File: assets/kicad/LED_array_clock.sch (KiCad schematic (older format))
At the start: 72 parts, among them U1 ULN2003A, U2 PIC16F628A, U3 74HC595, U4 74HC595

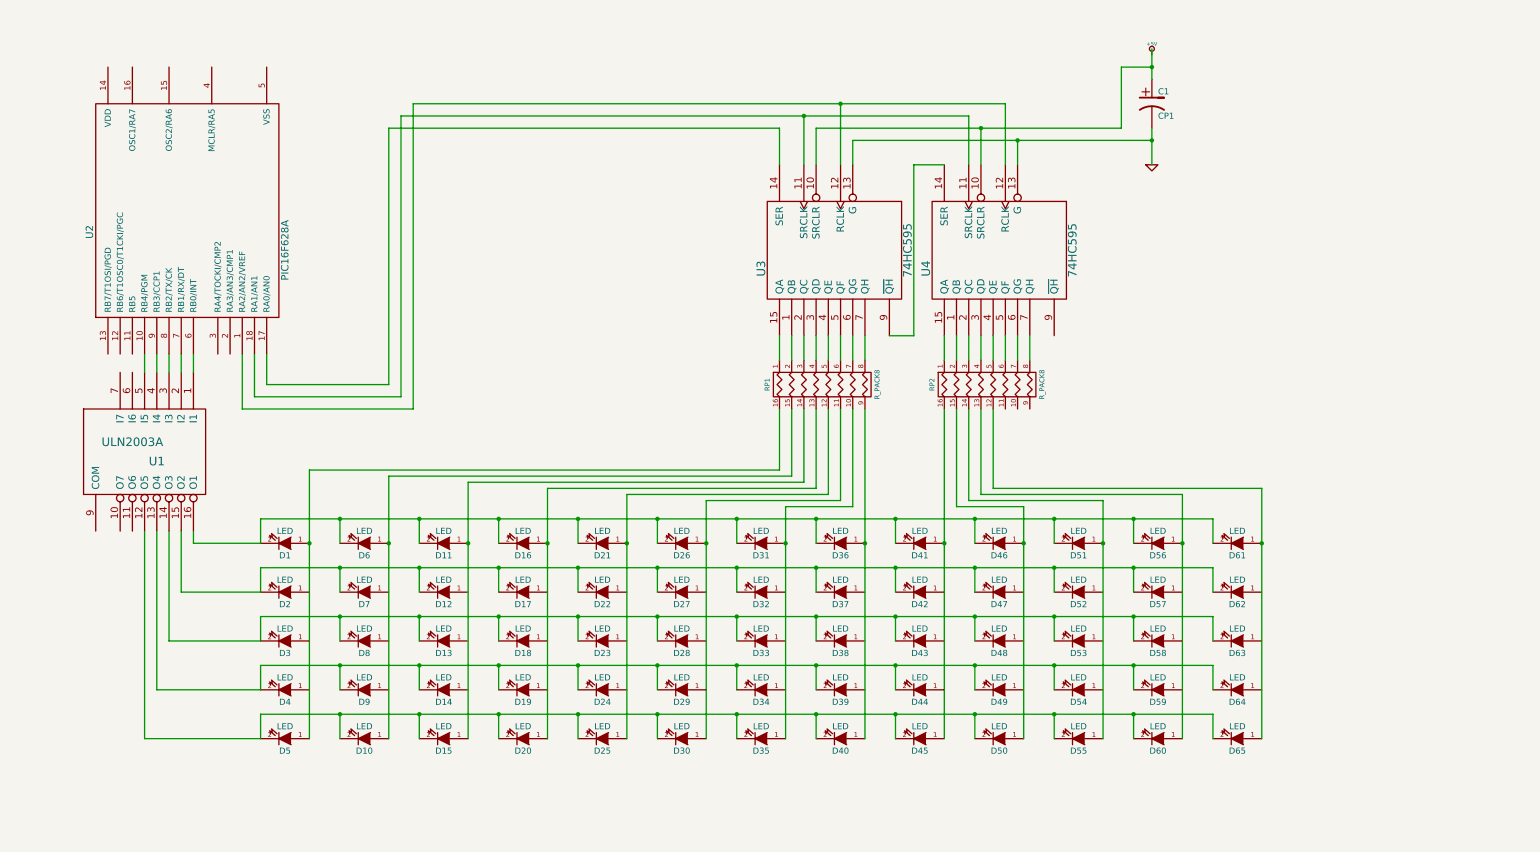
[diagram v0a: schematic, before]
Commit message: Added 3 matrix columns. Added RTC and interface components
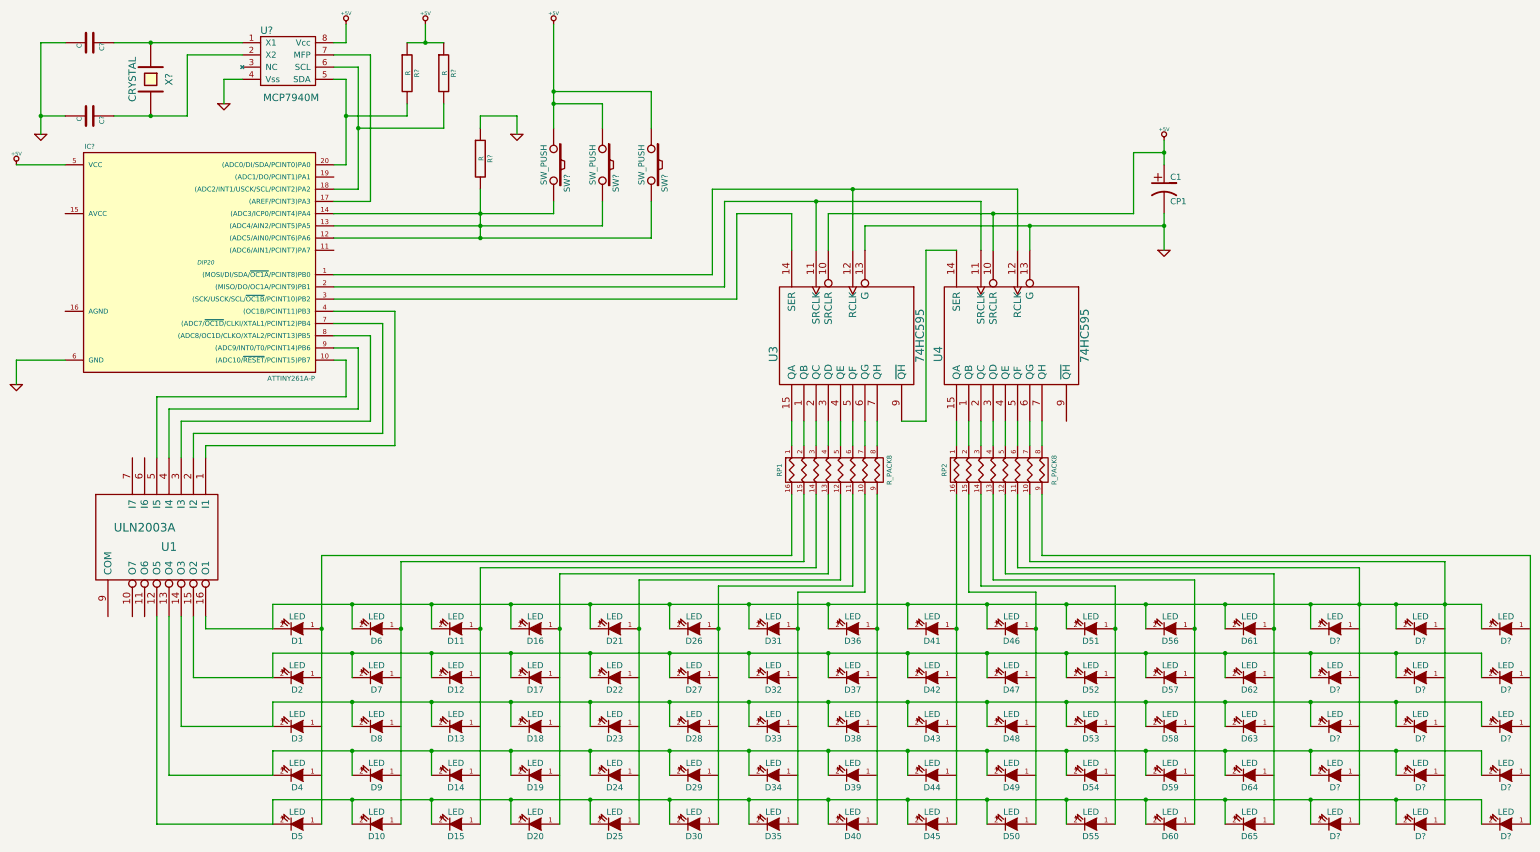
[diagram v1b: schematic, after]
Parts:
- removed U2: PIC16F628A, symbol PIC16F628A
- added C? (x2): C, ~, symbol C
- added D? (x15): LED, ~, symbol LED
- added IC?: ATTINY261A-P, DIP20, symbol ATTINY261A-P
- added R? (x3): R, ~, symbol R
- added SW? (x3): SW_PUSH, ~, symbol SW_PUSH
- added U?: MCP7940M, symbol MCP7940M
- added X?: CRYSTAL, ~, symbol CRYSTAL
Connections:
- net +5V: now also C1.1, U3.10 (SRCLR), U4.10 (SRCLR), IC?.5 (VCC), R?.1, R?.1, SW?.1, SW?.1, SW?.1, U?.8 (Vcc)
- net GND: now also C?.2, C?.2, IC?.6 (GND), R?.1, U?.4 (Vss)
- net at U3.11 (SRCLK), U4.11 (SRCLK): now also IC?.2 ((MISO/DO/OC1A/PCINT9)PB1)
- net at U3.12 (RCLK), U4.12 (RCLK): now also IC?.1 ((MOSI/DI/SDA/~OC1A~/PCINT8)PB0)
- net at U3.14 (SER): now also IC?.3 ((SCK/USCK/SCL/~OC1B~/PCINT10)PB2)
- net at D1.2 (K), D11.2 (K), D16.2 (K)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: now also RP2.10 (R7), RP2.11 (R6), D?.1 (A), D?.1 (A), D?.2 (K), D?.2 (K), D?.2 (K)
- net at D12.2 (K), D17.2 (K), D2.2 (K)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: now also D?.2 (K), D?.2 (K), D?.2 (K)
- net at D13.2 (K), D18.2 (K), D23.2 (K)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: now also D?.2 (K), D?.2 (K), D?.2 (K)
- net at D14.2 (K), D19.2 (K), D24.2 (K)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: now also D?.2 (K), D?.2 (K), D?.2 (K)
- net at D10.2 (K), D15.2 (K), D20.2 (K)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: now also D?.2 (K), D?.2 (K), D?.2 (K)
- net at RP2.9 (R8): now also D?.1 (A)
- net at U1.1 (I1): now also IC?.4 ((OC1B/PCINT11)PB3)
- net at U1.2 (I2): now also IC?.7 ((ADC7/~OC1D~/CLKI/XTAL1/PCINT12)PB4)
- net at U1.3 (I3): now also IC?.8 ((ADC8/OC1D/CLKO/XTAL2/PCINT13)PB5)
- net at U1.4 (I4): now also IC?.9 ((ADC9/INT0/T0/PCINT14)PB6)
- net at U1.5 (I5): now also IC?.10 ((ADC10/~RESET~/PCINT15)PB7)
- new net: IC?.12 ((ADC5/AIN0/PCINT6)PA6), IC?.13 ((ADC4/AIN2/PCINT5)PA5), IC?.14 ((ADC3/ICP0/PCINT4)PA4), R?.2, SW?.2, SW?.2, SW?.2
- new net: IC?.17 ((AREF/PCINT3)PA3), U?.7 (MFP)
- new net: IC?.18 ((ADC2/INT1/USCK/SCL/PCINT2)PA2), R?.2, U?.6 (SCL)
- new net: IC?.20 ((ADC0/DI/SDA/PCINT0)PA0), R?.2, U?.5 (SDA)
- new net: C?.1, U?.1 (X1), X?.1
- new net: C?.1, U?.2 (X2), X?.2
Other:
- moved on the sheet: C1, D1, D10, D11, D12, D13, D14, D15, D16, D17, D18, D19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

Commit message: Changed switches to pull-down. Cleaned up schematic
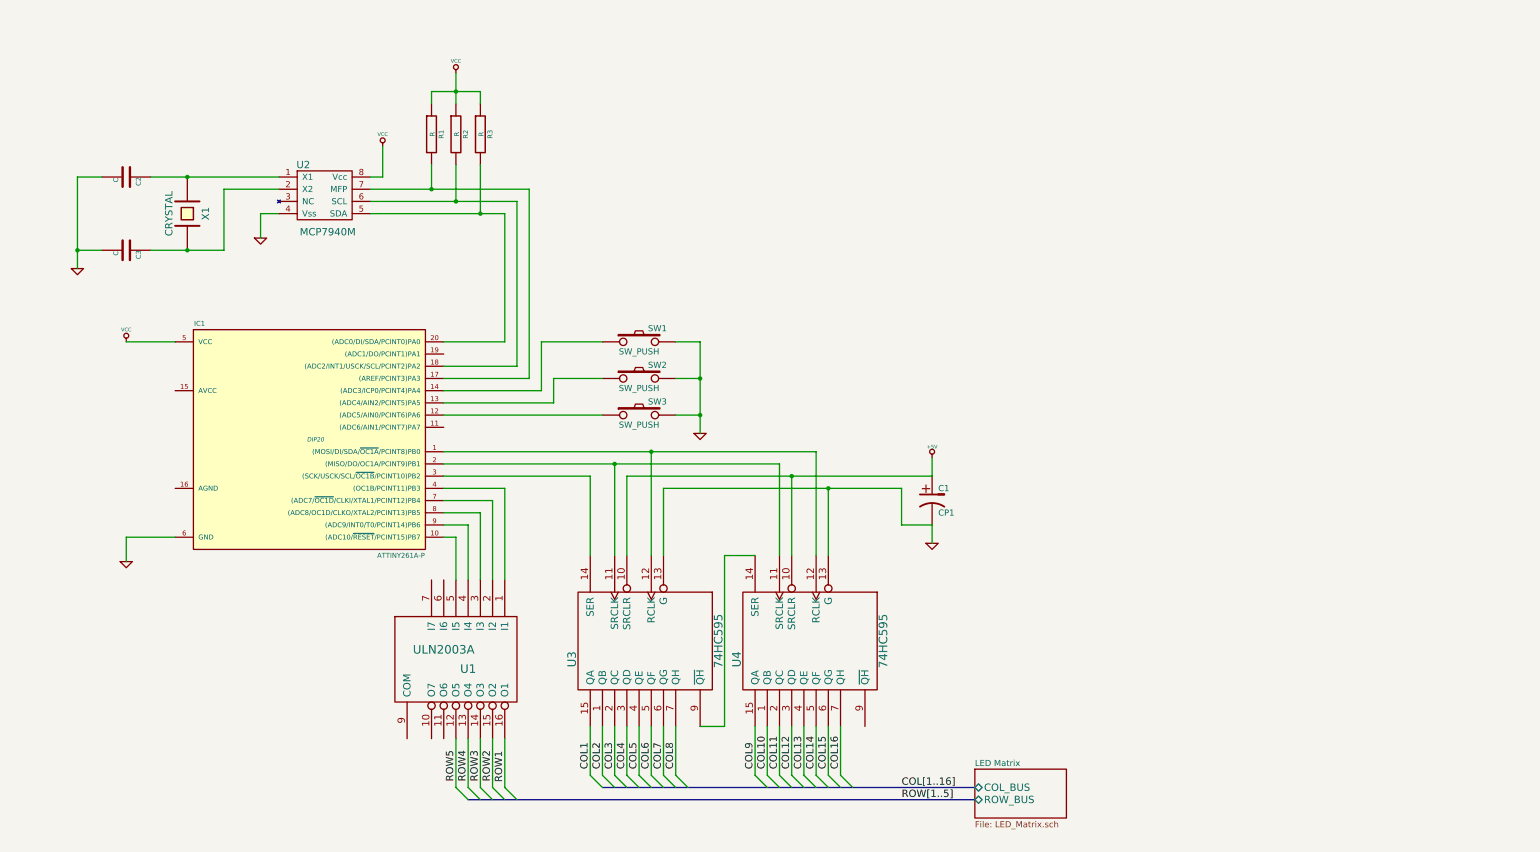
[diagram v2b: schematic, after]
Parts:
- removed C? (x2): C, ~, symbol C
- removed D1, D10, D11, D12, D13, D14, D15, D16, D17, D18, D19, D2, D20, D21, D22, D23, D24, D25, D26, D27, D28, D29, D3, D30, D31, D32, D33, D34, D35, D36, D37, D38, D39, D4, D40, D41, D42, D43, D44, D45, D46, D47, D48, D49, D5, D50, D51, D52, D53, D54, D55, D56, D57, D58, D59, D6, D60, D61, D62, D63, D64, D65, D7, D8, D9, D? (x15): LED, ~, symbol LED
- removed R? (x3): R, ~, symbol R
- removed RP1, RP2: R_PACK8, ~, symbol R_PACK8
- removed SW? (x3): SW_PUSH, ~, symbol SW_PUSH
- removed U?: MCP7940M, symbol MCP7940M
- removed X?: CRYSTAL, ~, symbol CRYSTAL
- added C2, C3: C, ~, symbol C
- added R1, R2, R3: R, ~, symbol R
- added SW1, SW2, SW3: SW_PUSH, ~, symbol SW_PUSH
- added U2: MCP7940M, symbol MCP7940M
- added X1: CRYSTAL, ~, symbol CRYSTAL
- gave numbers to parts that had none: 1
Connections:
- net +5V: no longer IC1.5 (VCC)
- net GND: now also C2.2, C3.2, SW1.2, SW2.2, SW3.2, U2.4 (Vss)
- net VCC: now also IC1.5 (VCC), R1.1, R2.1, R3.1, U2.8 (Vcc)
- net COL2: now reaches U3.1 (QB)
- net COL1: now reaches U3.15 (QA)
- net COL3: now reaches U3.2 (QC)
- net COL4: now reaches U3.3 (QD)
- net COL5: now reaches U3.4 (QE)
- net COL6: now reaches U3.5 (QF)
- net COL7: now reaches U3.6 (QG)
- net COL8: now reaches U3.7 (QH)
- net COL10: now reaches U4.1 (QB)
- net COL9: now reaches U4.15 (QA)
- net COL11: now reaches U4.2 (QC)
- net COL12: now reaches U4.3 (QD)
- net COL13: now reaches U4.4 (QE)
- net COL14: now reaches U4.5 (QF)
- net COL15: now reaches U4.6 (QG)
- net COL16: now reaches U4.7 (QH)
- net ROW1: now reaches U1.16 (O1)
- net ROW2: now reaches U1.15 (O2)
- net ROW3: now reaches U1.14 (O3)
- net ROW4: now reaches U1.13 (O4)
- net ROW5: now reaches U1.12 (O5)
- net at IC1.17 ((AREF/PCINT3)PA3): now also R1.2, U2.7 (MFP)
- net at IC1.18 ((ADC2/INT1/USCK/SCL/PCINT2)PA2): now also R2.2, U2.6 (SCL)
- net at IC1.20 ((ADC0/DI/SDA/PCINT0)PA0): now also R3.2, U2.5 (SDA)
- new net: IC1.12 ((ADC5/AIN0/PCINT6)PA6), SW3.1
- new net: IC1.13 ((ADC4/AIN2/PCINT5)PA5), SW2.1
- new net: IC1.14 ((ADC3/ICP0/PCINT4)PA4), SW1.1
- new net: C2.1, U2.1 (X1), X1.1
- new net: C3.1, U2.2 (X2), X1.2
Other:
- moved on the sheet: C1, IC1, U1, U3, U4

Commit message: Cleaned up schematic. Edited README for clarity.
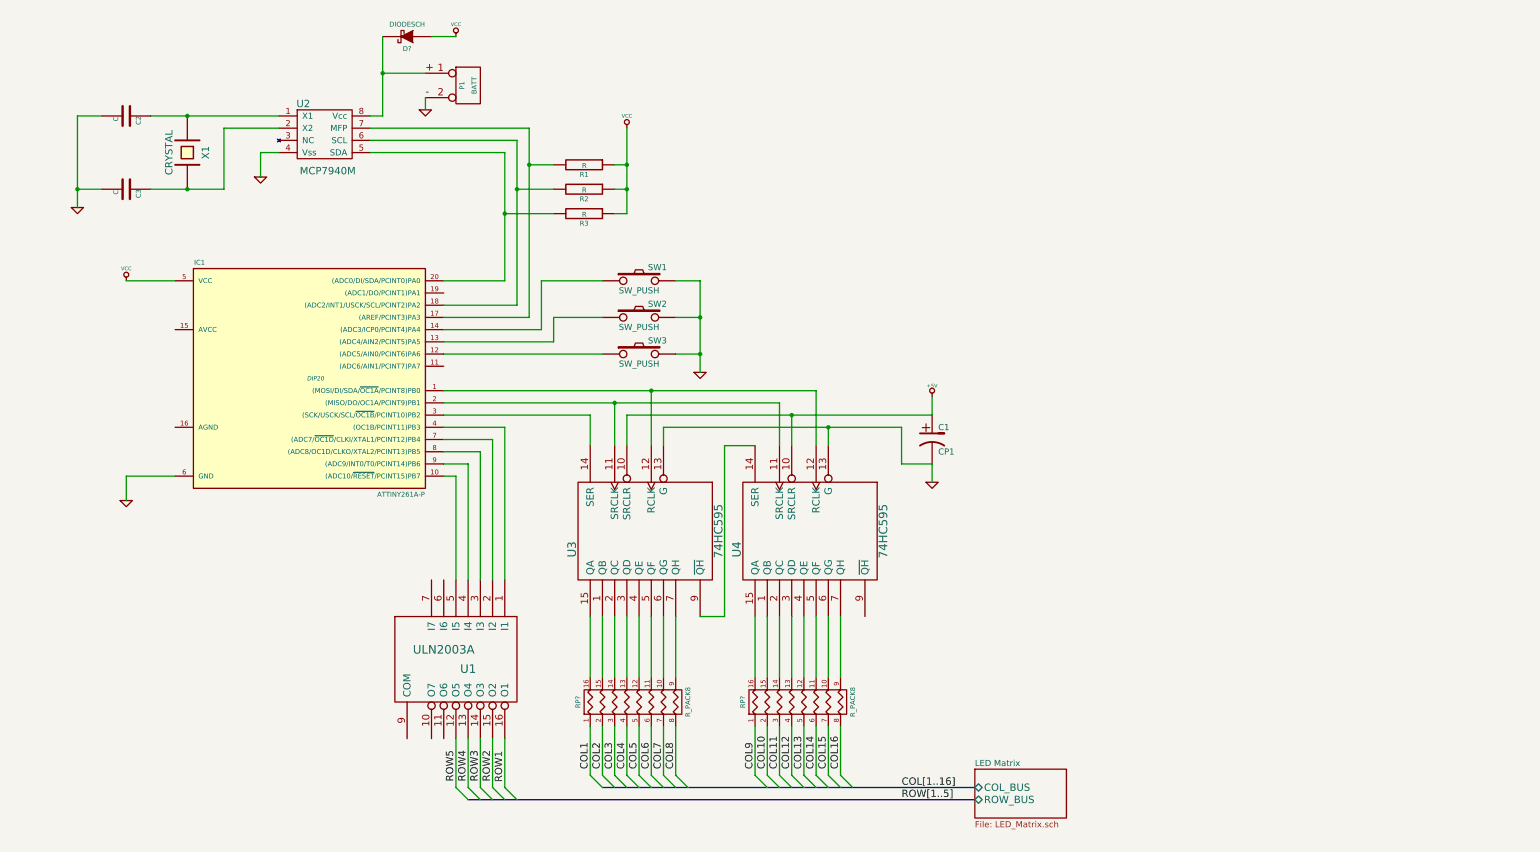
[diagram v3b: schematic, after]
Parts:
- added D?: DIODESCH, ~, symbol DIODESCH
- added P1: BATT, ~, symbol CONN_2
- added RP? (x2): R_PACK8, ~, symbol R_PACK8
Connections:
- net COL1: now also RP?.1 (P1); no longer U3.15 (QA)
- net COL10: now also RP?.2 (P2); no longer U4.1 (QB)
- net COL11: now also RP?.3 (P3); no longer U4.2 (QC)
- net COL12: now also RP?.4 (P4); no longer U4.3 (QD)
- net COL13: now also RP?.5 (P5); no longer U4.4 (QE)
- net COL14: now also RP?.6 (P6); no longer U4.5 (QF)
- net COL15: now also RP?.7 (P7); no longer U4.6 (QG)
- net COL16: now also RP?.8 (P8); no longer U4.7 (QH)
- net COL2: now also RP?.2 (P2); no longer U3.1 (QB)
- net COL3: now also RP?.3 (P3); no longer U3.2 (QC)
- net COL4: now also RP?.4 (P4); no longer U3.3 (QD)
- net COL5: now also RP?.5 (P5); no longer U3.4 (QE)
- net COL6: now also RP?.6 (P6); no longer U3.5 (QF)
- net COL7: now also RP?.7 (P7); no longer U3.6 (QG)
- net COL8: now also RP?.8 (P8); no longer U3.7 (QH)
- net COL9: now also RP?.1 (P1); no longer U4.15 (QA)
- net GND: now also P1.2 (PM)
- net VCC: now also D?.1 (A); no longer U2.8 (Vcc)
- new net: RP?.15 (R2), U3.1 (QB)
- new net: RP?.16 (R1), U3.15 (QA)
- new net: RP?.14 (R3), U3.2 (QC)
- new net: RP?.13 (R4), U3.3 (QD)
- new net: RP?.12 (R5), U3.4 (QE)
- new net: RP?.11 (R6), U3.5 (QF)
- new net: RP?.10 (R7), U3.6 (QG)
- new net: RP?.9 (R8), U3.7 (QH)
- new net: RP?.15 (R2), U4.1 (QB)
- new net: RP?.16 (R1), U4.15 (QA)
- new net: RP?.14 (R3), U4.2 (QC)
- new net: RP?.13 (R4), U4.3 (QD)
- new net: RP?.12 (R5), U4.4 (QE)
- new net: RP?.11 (R6), U4.5 (QF)
- new net: RP?.10 (R7), U4.6 (QG)
- new net: RP?.9 (R8), U4.7 (QH)
- new net +: D?.2 (K), P1.1 (P1), U2.8 (Vcc)
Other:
- moved on the sheet: C1, C2, C3, IC1, R1, R2, R3, SW1, SW2, SW3, U2, U3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
